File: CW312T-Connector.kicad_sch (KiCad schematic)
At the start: 19 parts, among them P1 PCIEx4 EDGE CONNECTOR, U1 LD1117STR

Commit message: draft updated, schematic draft done, pcb issues with size of board and fitting all parts on
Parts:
- removed R17: RES_1R1_0603, Resistor_SMD:R_0603_1608Metric, symbol 0603_Yageo_Res:RES_1R1_0603
- added R17: RES_1R_0805, Resistor_SMD:R_0805_2012Metric, symbol tutorial_2_library:RES_1R_0805
- renumbered U1 to U4
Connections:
- net 5V is gone; now on net +5V: C5.2, C6.2, U4.3 (VIN)
- net VCCINT_SHUNTLOW: now also R17.1
- net at C11.2, C12.2, JP5.2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: now also R17.2
- net HDR10: no longer names the net of P1.A18 (HDR10)
- net HDR5: no longer names the net of P1.A13 (HDR5)
- net HDR7: no longer names the net of P1.A15 (HDR7)
- net HDR8: no longer names the net of P1.A16 (HDR8)
- net HDR9: no longer names the net of P1.A17 (HDR9)
- net LED2: no longer names the net of P1.B12 (LED2)
- net LED3: no longer names the net of P1.B13 (LED3)
- no-connect marks 15 -> 22
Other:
- note added: "No connections to the other hdrs on the original schematic? -REMOVED"
- note added: "No other connections to LED2 or 3 on old schematic? -REMOVED"
- note removed: "CHANGE THIS RESISTOR SHOULD BE 1R0 also 0805 not 0603"
- moved on the sheet: R11, R18

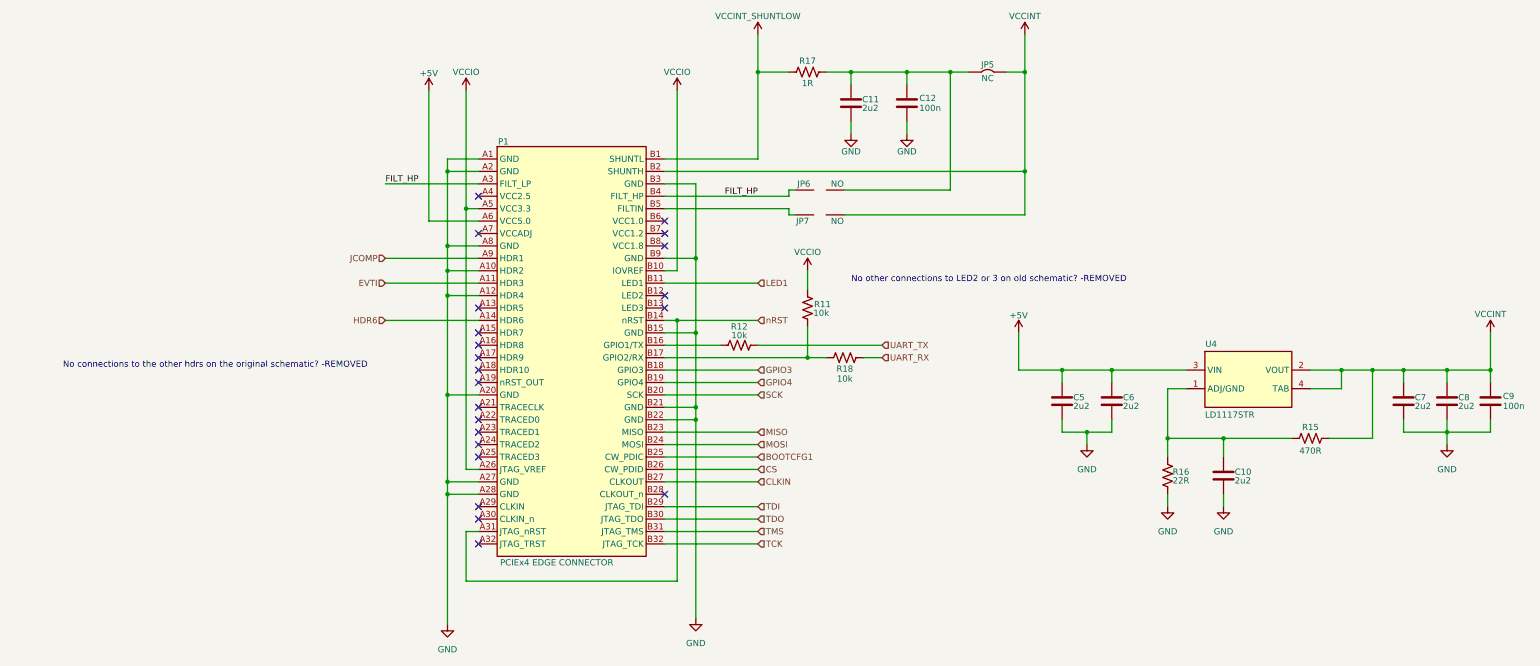
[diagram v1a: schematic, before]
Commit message: updated schematic after library re-organization
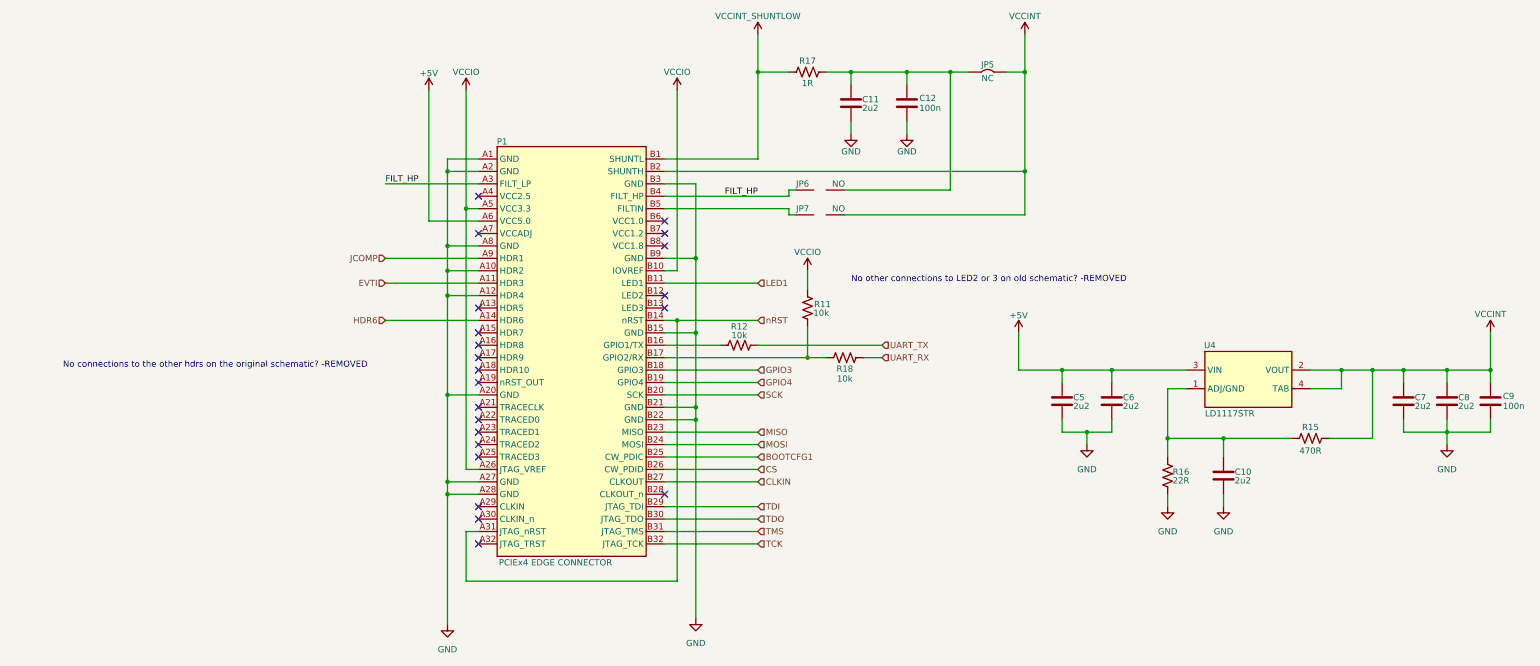
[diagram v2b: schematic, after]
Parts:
- removed JP6, JP7: ~, Jumper:SolderJumper-2_P1.3mm_Open_Pad1.0x1.5mm, symbol tutorial_2_library:Solder_Jumper_2_NO
- removed P1: PCIEx4 EDGE CONNECTOR, tutorial_2_library:CW312_Template, symbol tutorial_2_library:CW312T-Template
- removed U4: LD1117STR, Package_TO_SOT_SMD:SOT-223, symbol tutorial_2_library:LD1117STR
- added JP6, JP7: ~, Jumper:SolderJumper-2_P1.3mm_Open_Pad1.0x1.5mm, symbol NAE_Connectors:Solder_Jumper_2_NO
- added P1: PCIEx4 EDGE CONNECTOR, tutorial_2_library:CW312_Template, symbol NAE_Connectors:CW312T-Template
- added U4: LD1117STR, Package_TO_SOT_SMD:SOT-223, symbol NAE_Integrated_Circuits:LD1117STR
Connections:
- net +5V: now also P1.A6 (VCC5.0), U4.3 (VIN)
- net BOOTCFG1: now also P1.B25 (CW_PDIC)
- net CLKIN: now also P1.B27 (CLKOUT)
- net CS: now also P1.B26 (CW_PDID)
- net EVTI: now also P1.A11 (HDR3)
- net FILT_HP: now also JP6.2, P1.A3 (FILT_LP), P1.B4 (FILT_HP)
- net GND: now also P1.A1 (GND), P1.A10 (HDR2), P1.A12 (HDR4), P1.A2 (GND), P1.A20 (GND), P1.A27 (GND), P1.A28 (GND), P1.A8 (GND), P1.B15 (GND), P1.B21 (GND), P1.B22 (GND), P1.B3 (GND), P1.B9 (GND)
- net GPIO3: now also P1.B18 (GPIO3)
- net GPIO4: now also P1.B19 (GPIO4)
- net HDR6: now also P1.A14 (HDR6)
- net JCOMP: now also P1.A9 (HDR1)
- net LED1: now also P1.B11 (LED1)
- net MISO: now also P1.B23 (MISO)
- net MOSI: now also P1.B24 (MOSI)
- net SCK: now also P1.B20 (SCK)
- net TCK: now also P1.B32 (JTAG_TCK)
- net TDI: now also P1.B29 (JTAG_TDI)
- net TDO: now also P1.B30 (JTAG_TDO)
- net TMS: now also P1.B31 (JTAG_TMS)
- net VCCINT: now also JP7.1, P1.B2 (SHUNTH), U4.2 (VOUT), U4.4 (TAB)
- net VCCINT_SHUNTLOW: now also P1.B1 (SHUNTL)
- net VCCIO: now also P1.A26 (JTAG_VREF), P1.A5 (VCC3.3), P1.B10 (IOVREF)
- net nRST: now also P1.A31 (JTAG_nRST), P1.B14 (nRST)
- net at C10.2, R15.1, R16.2: now also U4.1 (ADJ/GND)
- net at C11.2, C12.2, JP5.2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: now also JP6.1
- net at R11.1, R18.1: now also P1.B17 (GPIO2/RX)
- net at R12.1: now also P1.B16 (GPIO1/TX)
- new net: JP7.2, P1.B5 (FILTIN)
